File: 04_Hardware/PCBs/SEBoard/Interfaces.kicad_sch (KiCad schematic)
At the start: 66 parts, among them J12 67996-100HLF, J2 10-89-7121, Q1 BC847C,215, Q10 BC817-40,215, Q2 BC847C,215, Q3 BC847C,215, Q4 BC817-40,215, Q5 BC817-40,215, Q6 BC817-40,215, Q7 BC817-40,215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

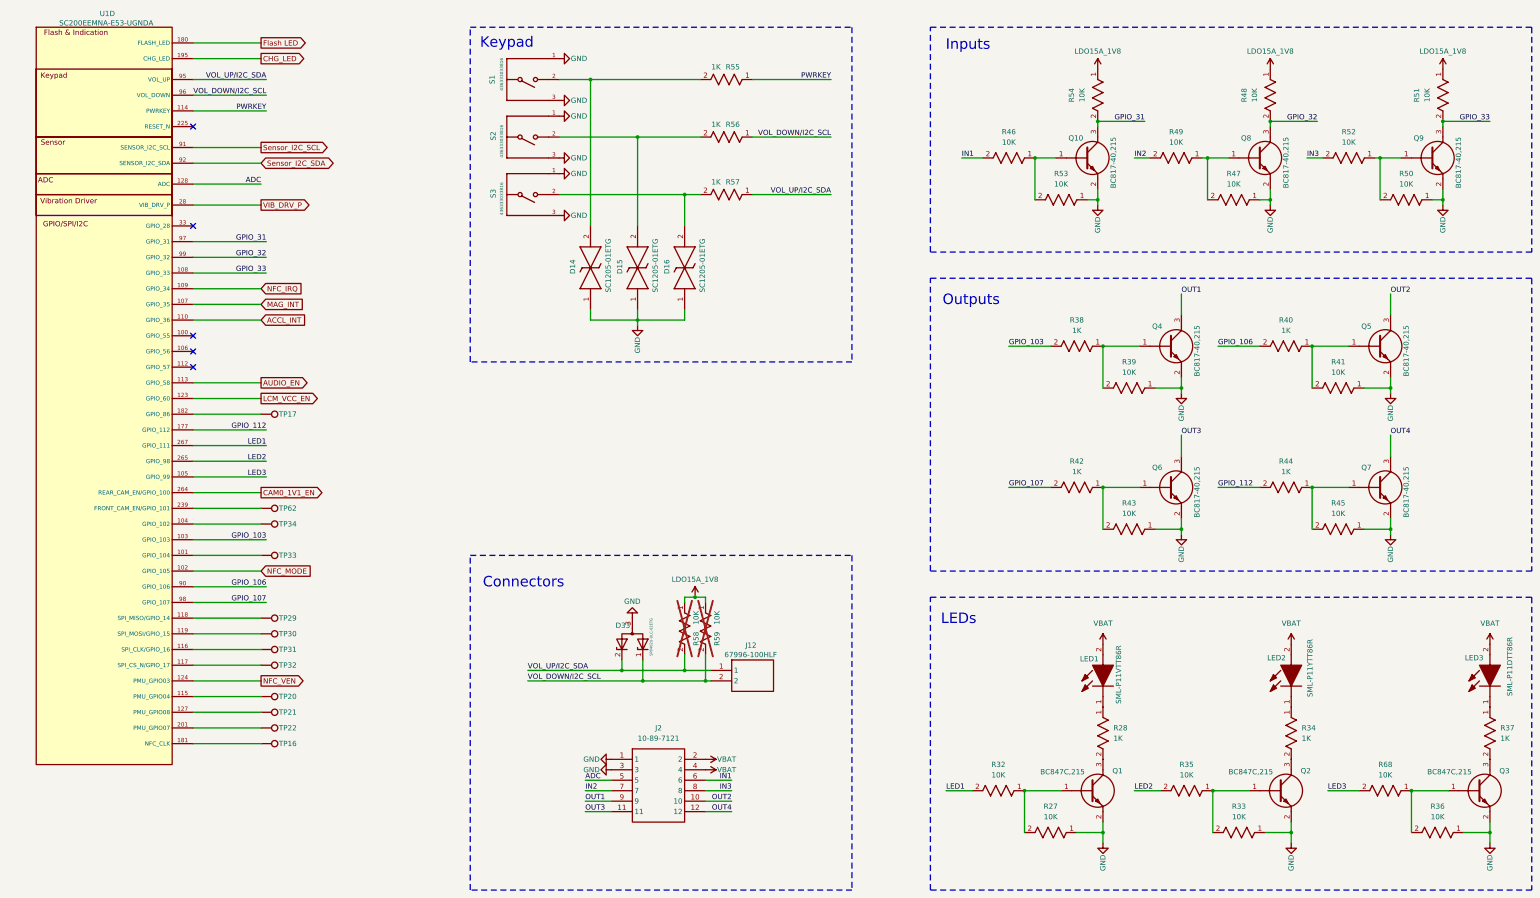
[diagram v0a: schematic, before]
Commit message: feat(schematic): add SE250B4 symbol to schematic (unchecked)
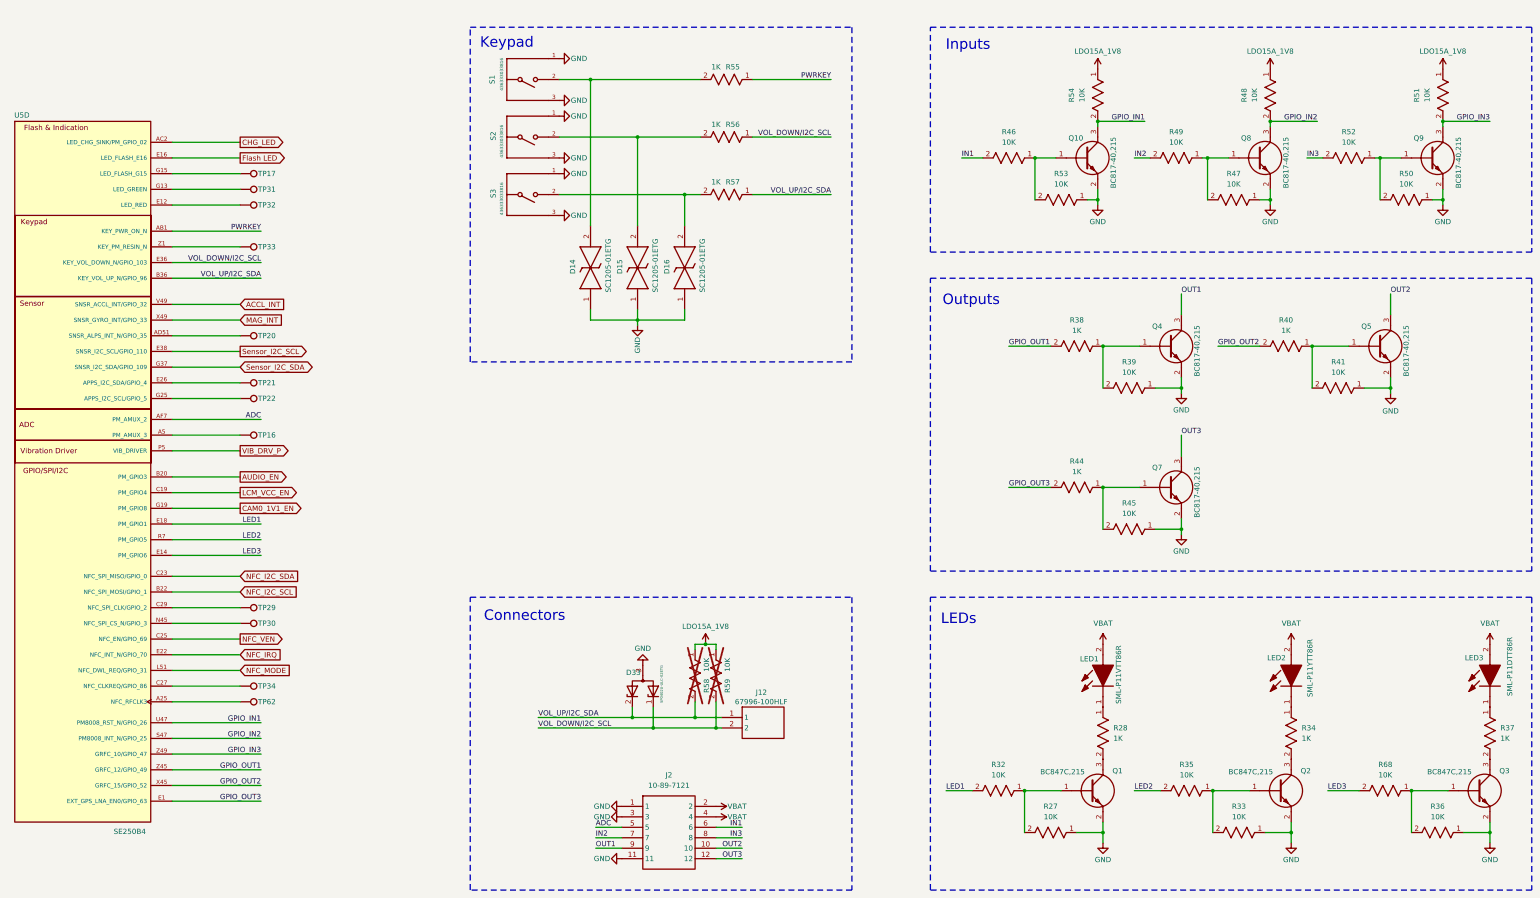
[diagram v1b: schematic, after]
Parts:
- removed Q6: BC817-40,215, SEBoard:BC81740215, symbol SEBoard:BC817-40,215
- removed R42: 1K, SEBoard:RC0402N_YAG, symbol SEBoard:RC0402JR-071KL
- removed R43: 10K, SEBoard:RC0402N_YAG, symbol SEBoard:RC0402JR-0710KL
- removed U1: SC200EEMNA-E53-UGNDA, SEBoard:SC200E_SC206E, symbol SEBoard:SC200E
- added U5: SE250B4, 000MCLib:XCVR_SE250B4-NA, symbol 000MCLib:SE250B4
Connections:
- net OUT4 is gone; now on net OUT3: J2.12, Q7.3 (C)
- net ACCL_INT: now also U5.V49 (SNSR_ACCL_INT/GPIO_32)
- net ADC: now also U5.AF7 (PM_AMUX_2)
- net AUDIO_EN: now also U5.B20 (PM_GPIO3)
- net CAM0_1V1_EN: now also U5.G19 (PM_GPIO8)
- net CHG_LED: now also U5.AC2 (LED_CHG_SINK/PM_GPIO_02)
- net Flash LED: now also U5.E16 (LED_FLASH_E16)
- net GND: now also J2.11
- net LCM_VCC_EN: now also U5.C19 (PM_GPIO4)
- net LED1: now also U5.E18 (PM_GPIO1)
- net LED2: now also U5.R7 (PM_GPIO5)
- net LED3: now also U5.E14 (PM_GPIO6)
- net MAG_INT: now also U5.X49 (SNSR_GYRO_INT/GPIO_33)
- net NFC_IRQ: now also U5.E22 (NFC_INT_N/GPIO_70)
- net NFC_MODE: now also U5.L51 (NFC_DWL_REQ/GPIO_31)
- net NFC_VEN: now also U5.C25 (NFC_EN/GPIO_69)
- net OUT3: no longer J2.11
- net PWRKEY: now also U5.AB1 (KEY_PWR_ON_N)
- net Sensor_I2C_SCL: now also U5.E38 (SNSR_I2C_SCL/GPIO_110)
- net Sensor_I2C_SDA: now also U5.G37 (SNSR_I2C_SDA/GPIO_109)
- net VIB_DRV_P: now also U5.P5 (VIB_DRIVER)
- net VOL_DOWN/I2C_SCL: now also U5.E36 (KEY_VOL_DOWN_N/GPIO_103)
- net VOL_UP/I2C_SDA : now also U5.B36 (KEY_VOL_UP_N/GPIO_96)
- net at TP33.1: now also U5.Z1 (KEY_PM_RESIN_N)
- net at TP62.1: now also U5.A25 (NFC_RFCLK3)
- net at TP34.1: now also U5.C27 (NFC_CLKREQ/GPIO_86)
- net at TP20.1: now also U5.AD51 (SNSR_ALPS_INT_N/GPIO_35)
- net at TP31.1: now also U5.G13 (LED_GREEN)
- net at TP32.1: now also U5.E12 (LED_RED)
- net at TP29.1: now also U5.C29 (NFC_SPI_CLK/GPIO_2)
- net at TP30.1: now also U5.N45 (NFC_SPI_CS_N/GPIO_3)
- net at TP21.1: now also U5.E26 (APPS_I2C_SDA/GPIO_4)
- net at TP16.1: now also U5.A5 (PM_AMUX_3)
- net at TP17.1: now also U5.G15 (LED_FLASH_G15)
- net at TP22.1: now also U5.G25 (APPS_I2C_SCL/GPIO_5)
- net GPIO_103 renamed GPIO_OUT1
- net GPIO_OUT1: now also U5.Z45 (GRFC_12/GPIO_49)
- net GPIO_106 renamed GPIO_OUT2
- net GPIO_OUT2: now also U5.X45 (GRFC_15/GPIO_52)
- net GPIO_112 renamed GPIO_OUT3
- net GPIO_OUT3: now also U5.E1 (EXT_GPS_LNA_EN0/GPIO_63)
- net GPIO_31 renamed GPIO_IN1
- net GPIO_IN1: now also U5.U47 (PM8008_RST_N/GPIO_26)
- net GPIO_32 renamed GPIO_IN2
- net GPIO_IN2: now also U5.S47 (PM8008_INT_N/GPIO_25)
- net GPIO_33 renamed GPIO_IN3
- net GPIO_IN3: now also U5.Z49 (GRFC_10/GPIO_47)
- new net NFC_I2C_SCL: U5.B22 (NFC_SPI_MOSI/GPIO_1)
- new net NFC_I2C_SDA: U5.C23 (NFC_SPI_MISO/GPIO_0)
- no-connect marks 5 -> 0
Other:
- moved on the sheet: D33, J12, J2, Q7, R44, R45, R58, R59, TP16, TP17, TP20, TP21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

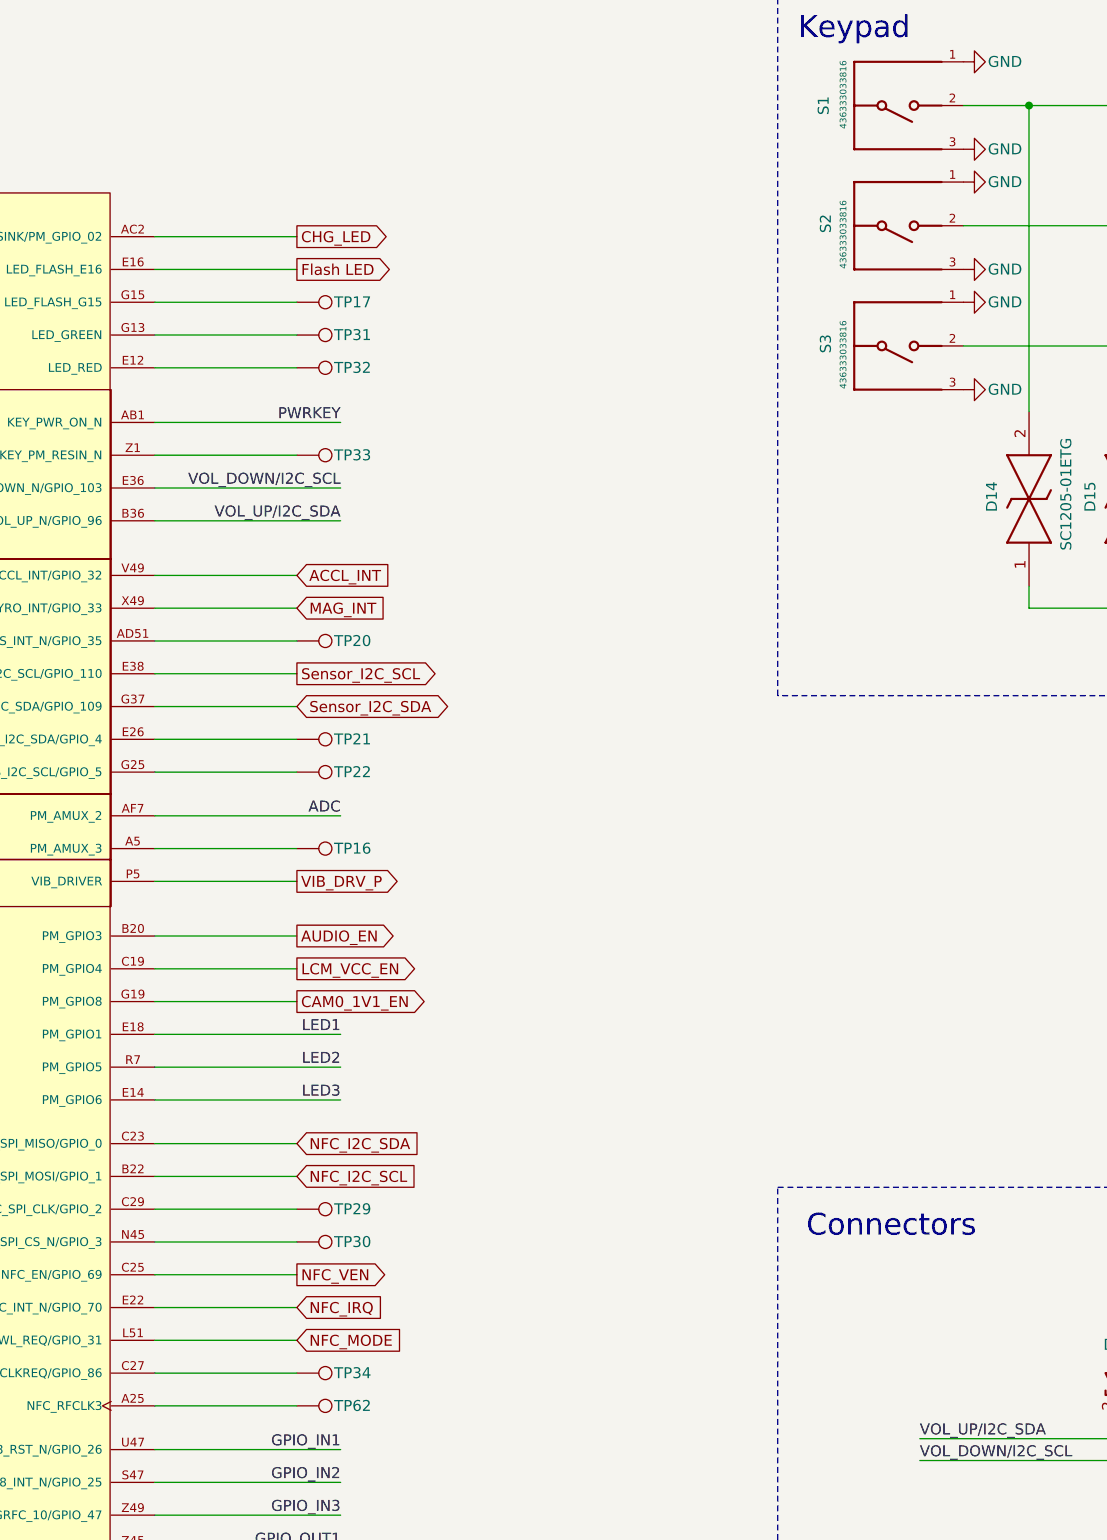
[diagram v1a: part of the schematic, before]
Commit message: feat: Updated schematic layout and moved new components to Layout
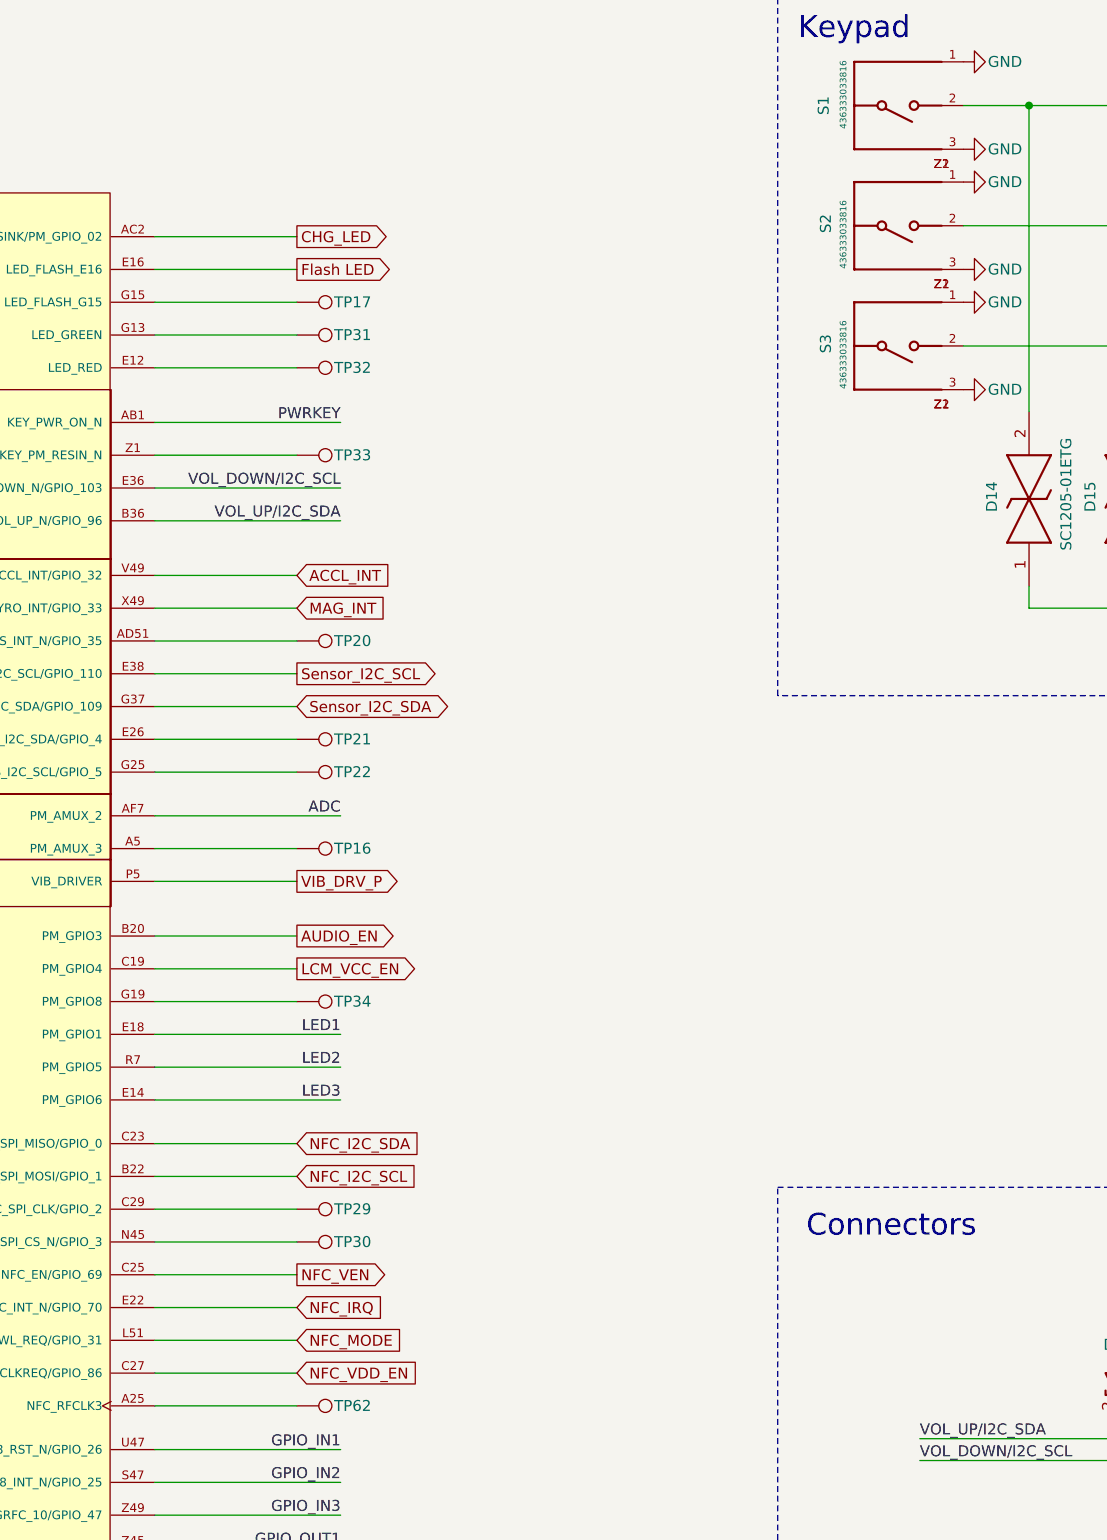
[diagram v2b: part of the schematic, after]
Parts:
- removed TP34: Sens_M, TestPoint:TestPoint_Pad_D1.0mm, symbol SEBoard:TestPoint
- added TP34: Sens_M, TestPoint:TestPoint_Pad_D1.0mm, symbol 000MCLib:TestPoint
- D14, D15, D16: footprint SEBoard:SC120501ETG -> 000MCLib:SC120501ETG; symbol SEBoard:SC1205-01ETG -> 000MCLib:SC1205-01ETG
- D33: footprint SEBoard:SESD0402Q2UG0020090 -> 000MCLib:SESD0402Q2UG0020090; symbol SEBoard:SP0402U-ULC-02ETG -> 000MCLib:SP0402U-ULC-02ETG
- J12: footprint SEBoard:HDRV2W67P254_2X1_254X483X858P -> 000MCLib:HDRV2W67P254_2X1_254X483X858P; symbol SEBoard:67996-100HLF -> 000MCLib:67996-100HLF
- J2: footprint SEBoard:HDRV12W87P254X254_2X6 -> 000MCLib:HDRV12W87P254X254_2X6; symbol SEBoard:10-89-7121 -> 000MCLib:10-89-7121
- LED1: footprint SEBoard:SMLP11VTT86R -> 000MCLib:SMLP11VTT86R; symbol SEBoard:SML-P11VTT86R -> 000MCLib:SML-P11VTT86R
- LED2: footprint SEBoard:SMLP11VTT86R -> 000MCLib:SMLP11VTT86R; symbol SEBoard:SML-P11YTT86R -> 000MCLib:SML-P11YTT86R
- LED3: footprint SEBoard:SMLP11VTT86R -> 000MCLib:SMLP11VTT86R; symbol SEBoard:SML-P11DTT86R -> 000MCLib:SML-P11DTT86R
- Q1, Q2, Q3: footprint SOT95P230X110-3N -> 000MCLib:SOT95P230X110-3N; symbol SEBoard:BC847C,215 -> 000MCLib:BC847C,215
- Q10, Q4, Q5, Q7, Q8, Q9: footprint SEBoard:BC81740215 -> 000MCLib:BC81740215; symbol SEBoard:BC817-40,215 -> 000MCLib:BC817-40,215
- R27, R32, R33, R35, R36, R39, R41, R45, R46, R47, R48, R49, R50, R51, R52, R53, R54, R58, R59, R68: footprint SEBoard:RC0402N_YAG -> 000MCLib:RC0402N_YAG; symbol SEBoard:RC0402JR-0710KL -> 000MCLib:RC0402JR-0710KL
- R28, R34, R37, R38, R40, R44, R55, R56, R57: footprint SEBoard:RC0402N_YAG -> 000MCLib:RC0402N_YAG; symbol SEBoard:RC0402JR-071KL -> 000MCLib:RC0402JR-071KL
- S1, S2, S3: footprint SEBoard:436333033816 -> 000MCLib:436333033816; symbol SEBoard:436333033816 -> 000MCLib:436333033816
- TP16, TP17, TP20, TP21, TP22, TP29, TP30, TP31, TP32, TP33, TP62: symbol SEBoard:TestPoint -> 000MCLib:TestPoint
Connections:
- net NFC_VDD_EN: now reaches U5.C27 (NFC_CLKREQ/GPIO_86)
- net CAM0_1V1_EN: no longer names the net of U5.G19 (PM_GPIO8)
- net CAM0_1V1_EN: now also TP34.1
- new net: S2.Z1, S2.Z2
- new net: S1.Z1, S1.Z2
- new net: S3.Z1, S3.Z2
